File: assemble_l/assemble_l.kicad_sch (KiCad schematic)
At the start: 45 parts, among them J1 Conn_01x02_Pin, SW1 SW_Push, SW10 SW_Push, SW11 SW_Push, SW12 SW_Push, SW13 SW_Push, SW14 SW_Push, SW15 SW_Push, SW16 SW_Push, SW17 SW_Push, SW18 SW_Push, SW19 SW_Push, SW2 SW_Push, SW20 SW_Push, SW21 SW_Push, SW22 SW_Push, SW3 SW_Push, SW4 SW_Push, SW5 SW_Push, SW6 SW_Push, SW7 SW_Push, SW8 SW_Push, SW9 SW_Push, U1 Micon_BLEMicroPro

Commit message: fix: re-change layout
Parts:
- renumbered D9 to D3, D3 to D4, D4 to D5, D5 to D6, D6 to D7, D7 to D8, D8 to D9, SW9 to SW3, SW3 to SW4, SW4 to SW5, SW5 to SW6, SW6 to SW7, SW7 to SW8, SW8 to SW9
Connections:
- net Col0: now also SW3.1
- net Col2: no longer SW3.1
- net Row2: now also D3.1 (K)
- net Row3: no longer D3.1 (K)
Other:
- moved on the sheet: D3, SW3
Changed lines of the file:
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@@
 	)
 	(junction
+		(at 60.96 137.16)
+		(diameter 0)
+		(color 0 0 0 0)
+	)
+	(junction
 		(at 21.59 33.02)
 		(diameter 0)
@@
 	)
 	(junction
-		(at 99.06 158.75)
-		(diameter 0)
-		(color 0 0 0 0)
-	)
-	(junction
 		(at 137.16 158.75)
 		(diameter 0)
@@
 	)
 	(junction
-		(at 88.9 129.54)
+		(at 50.8 113.03)
 		(diameter 0)
 		(color 0 0 0 0)
@@
 	(wire
 		(pts
-			(xy 34.29 137.16) (xy 80.01 137.16)
+			(xy 34.29 137.16) (xy 60.96 137.16)
 		)
 		(stroke
@@
 	(wire
 		(pts
-			(xy 34.29 158.75) (xy 99.06 158.75)
+			(xy 50.8 113.03) (xy 50.8 129.54)
 		)
 		(stroke
@@
 	(wire
 		(pts
-			(xy 121.92 120.65) (xy 137.16 120.65)
+			(xy 34.29 158.75) (xy 121.92 158.75)
 		)
 		(stroke
@@
 	(wire
 		(pts
-			(xy 88.9 129.54) (xy 88.9 147.32)
+			(xy 121.92 120.65) (xy 137.16 120.65)
 		)
 		(stroke
@@
 	(wire
 		(pts
-			(xy 99.06 158.75) (xy 121.92 158.75)
-		)
-		(stroke
-			(width 0)
-			(type default)
-		)
-	)
-	(wire
-		(pts
 			(xy 50.8 93.98) (xy 50.8 113.03)
 		)
@@
 	(wire
 		(pts
-			(xy 99.06 154.94) (xy 99.06 158.75)
+			(xy 60.96 101.6) (xy 80.01 101.6)
 		)
 		(stroke
@@
 	(wire
 		(pts
-			(xy 60.96 101.6) (xy 80.01 101.6)
+			(xy 99.06 137.16) (xy 121.92 137.16)
 		)
 		(stroke
@@
 	(wire
 		(pts
-			(xy 99.06 137.16) (xy 121.92 137.16)
+			(xy 21.59 22.86) (xy 21.59 30.48)
 		)
 		(stroke
@@
 	(wire
 		(pts
-			(xy 21.59 22.86) (xy 21.59 30.48)
+			(xy 137.16 158.75) (xy 153.67 158.75)
 		)
 		(stroke
@@
 	(wire
 		(pts
-			(xy 137.16 158.75) (xy 153.67 158.75)
+			(xy 69.85 93.98) (xy 69.85 113.03)
 		)
 		(stroke
@@
 	(wire
 		(pts
-			(xy 69.85 93.98) (xy 69.85 113.03)
+			(xy 60.96 137.16) (xy 80.01 137.16)
 		)
 		(stroke
@@
 		(dnp no)
 		(fields_autoplaced yes)
-		(property "Reference" "SW8"
+		(property "Reference" "SW9"
 			(at 93.98 121.92 0)
 			(effects
@@
 			(project "wikbd_assemble_l"
 				(path "/d117cd26-8e7e-4c35-b450-26176f9e2abc"
-					(reference "SW8")
+					(reference "SW9")
 					(unit 1)
 				)
@@
 	(symbol
 		(lib_id "Switch:SW_Push")
-		(at 93.98 147.32 0)
+		(at 55.88 129.54 0)
 		(unit 1)
 		(exclude_from_sim no)
@@
 		(dnp no)
 		(fields_autoplaced yes)
-		(property "Reference" "SW9"
-			(at 93.98 139.7 0)
+		(property "Reference" "SW3"
+			(at 55.88 121.92 0)
 			(effects
 				(font
@@
 		)
 		(property "Value" "SW_Push"
-			(at 93.98 142.24 0)
+			(at 55.88 124.46 0)
 			(effects
 				(font
@@
 		)
 		(property "Footprint" "kbd_SW:Choc_v2_Hotswap_1u_16.5"
-			(at 93.98 142.24 0)
+			(at 55.88 124.46 0)
 			(effects
 				(font
@@
 		)
 		(property "Datasheet" "~"
-			(at 93.98 142.24 0)
+			(at 55.88 124.46 0)
 			(effects
 				(font
@@
 		)
 		(property "Description" "Push button switch, generic, two pins"
-			(at 93.98 147.32 0)
+			(at 55.88 129.54 0)
 			(effects
 				(font
@@
 			(project "wikbd_assemble_l"
 				(path "/d117cd26-8e7e-4c35-b450-26176f9e2abc"
-					(reference "SW9")
+					(reference "SW3")
 					(unit 1)
 				)
@@
 		(dnp no)
 		(fields_autoplaced yes)
-		(property "Reference" "D8"
+		(property "Reference" "D9"
 			(at 101.6 132.0799 90)
 			(effects
@@
 			(project "wikbd_assemble_l"
 				(path "/d117cd26-8e7e-4c35-b450-26176f9e2abc"
-					(reference "D8")
+					(reference "D9")
 					(unit 1)
 				)
@@
 		(dnp no)
 		(fields_autoplaced yes)
-		(property "Reference" "D6"
+		(property "Reference" "D7"
 			(at 101.6 96.5199 90)
 			(effects
@@
 			(project "wikbd_assemble_l"
 				(path "/d117cd26-8e7e-4c35-b450-26176f9e2abc"
-					(reference "D6")
+					(reference "D7")
 					(unit 1)
 				)
@@
 		(dnp no)
 		(fields_autoplaced yes)
-		(property "Reference" "D5"
+		(property "Reference" "D6"
 			(at 82.55 132.0799 90)
 			(effects
@@
 			(project "wikbd_assemble_l"
 				(path "/d117cd26-8e7e-4c35-b450-26176f9e2abc"
-					(reference "D5")
+					(reference "D6")
 					(unit 1)
 				)
@@
 		(dnp no)
 		(fields_autoplaced yes)
-		(property "Reference" "SW3"
+		(property "Reference" "SW4"
 			(at 74.93 86.36 0)
 			(effects
@@
 			(project "wikbd_assemble_l"
 				(path "/d117cd26-8e7e-4c35-b450-26176f9e2abc"
-					(reference "SW3")
+					(reference "SW4")
 					(unit 1)
 				)
@@
 		(dnp no)
 		(fields_autoplaced yes)
-		(property "Reference" "SW6"
+		(property "Reference" "SW7"
 			(at 93.98 86.36 0)
 			(effects
@@
 			(project "wikbd_assemble_l"
 				(path "/d117cd26-8e7e-4c35-b450-26176f9e2abc"
-					(reference "SW6")
+					(reference "SW7")
 					(unit 1)
 				)
@@
 	(symbol
 		(lib_id "Device:D")
-		(at 99.06 151.13 90)
+		(at 60.96 133.35 90)
 		(unit 1)
 		(exclude_from_sim no)
@@
 		(dnp no)
 		(fields_autoplaced yes)
-		(property "Reference" "D9"
-			(at 101.6 149.8599 90)
+		(property "Reference" "D3"
+			(at 63.5 132.0799 90)
 			(effects
 				(font
@@
 		)
 		(property "Value" "D"
-			(at 101.6 152.3999 90)
+			(at 63.5 134.6199 90)
 			(effects
 				(font
@@
 		)
 		(property "Footprint" "kbd_Parts:Diode_TH_SMD"
-			(at 99.06 151.13 0)
+			(at 60.96 133.35 0)
 			(effects
 				(font
@@
 		)
 		(property "Datasheet" "~"
-			(at 99.06 151.13 0)
+			(at 60.96 133.35 0)
 			(effects
 				(font
@@
 		)
 		(property "Description" "Diode"
-			(at 99.06 151.13 0)
+			(at 60.96 133.35 0)
 			(effects
 				(font
@@
 		)
 		(property "Sim.Device" "D"
-			(at 99.06 151.13 0)
+			(at 60.96 133.35 0)
 			(effects
 				(font
@@
 		)
 		(property "Sim.Pins" "1=K 2=A"
-			(at 99.06 151.13 0)
+			(at 60.96 133.35 0)
 			(effects
 				(font
@@
 			(project "wikbd_assemble_l"
 				(path "/d117cd26-8e7e-4c35-b450-26176f9e2abc"
-					(reference "D9")
+					(reference "D3")
 					(unit 1)
 				)
@@
 		(dnp no)
 		(fields_autoplaced yes)
-		(property "Reference" "SW5"
+		(property "Reference" "SW6"
 			(at 74.93 121.92 0)
 			(effects
@@
 			(project "wikbd_assemble_l"
 				(path "/d117cd26-8e7e-4c35-b450-26176f9e2abc"
-					(reference "SW5")
+					(reference "SW6")
 					(unit 1)
 				)
@@
 		(dnp no)
 		(fields_autoplaced yes)
-		(property "Reference" "SW4"
+		(property "Reference" "SW5"
 			(at 74.93 105.41 0)
 			(effects
@@
 			(project "wikbd_assemble_l"
 				(path "/d117cd26-8e7e-4c35-b450-26176f9e2abc"
-					(reference "SW4")
+					(reference "SW5")
 					(unit 1)
 				)
@@
 		(dnp no)
 		(fields_autoplaced yes)
-		(property "Reference" "SW7"
+		(property "Reference" "SW8"
 			(at 93.98 105.41 0)
 			(effects
@@
 			(project "wikbd_assemble_l"
 				(path "/d117cd26-8e7e-4c35-b450-26176f9e2abc"
-					(reference "SW7")
+					(reference "SW8")
 					(unit 1)
 				)
@@
 		(dnp no)
 		(fields_autoplaced yes)
-		(property "Reference" "D3"
+		(property "Reference" "D4"
 			(at 82.55 96.5199 90)
 			(effects
@@
 			(project "wikbd_assemble_l"
 				(path "/d117cd26-8e7e-4c35-b450-26176f9e2abc"
-					(reference "D3")
+					(reference "D4")
 					(unit 1)
 				)
@@
 		(dnp no)
 		(fields_autoplaced yes)
-		(property "Reference" "D7"
+		(property "Reference" "D8"
 			(at 101.6 115.5699 90)
 			(effects
@@
 			(project "wikbd_assemble_l"
 				(path "/d117cd26-8e7e-4c35-b450-26176f9e2abc"
-					(reference "D7")
+					(reference "D8")
 					(unit 1)
 				)
@@
 		(dnp no)
 		(fields_autoplaced yes)
-		(property "Reference" "D4"
+		(property "Reference" "D5"
 			(at 82.55 115.5699 90)
 			(effects
@@
 			(project "wikbd_assemble_l"
 				(path "/d117cd26-8e7e-4c35-b450-26176f9e2abc"
-					(reference "D4")
+					(reference "D5")
 					(unit 1)
 				)

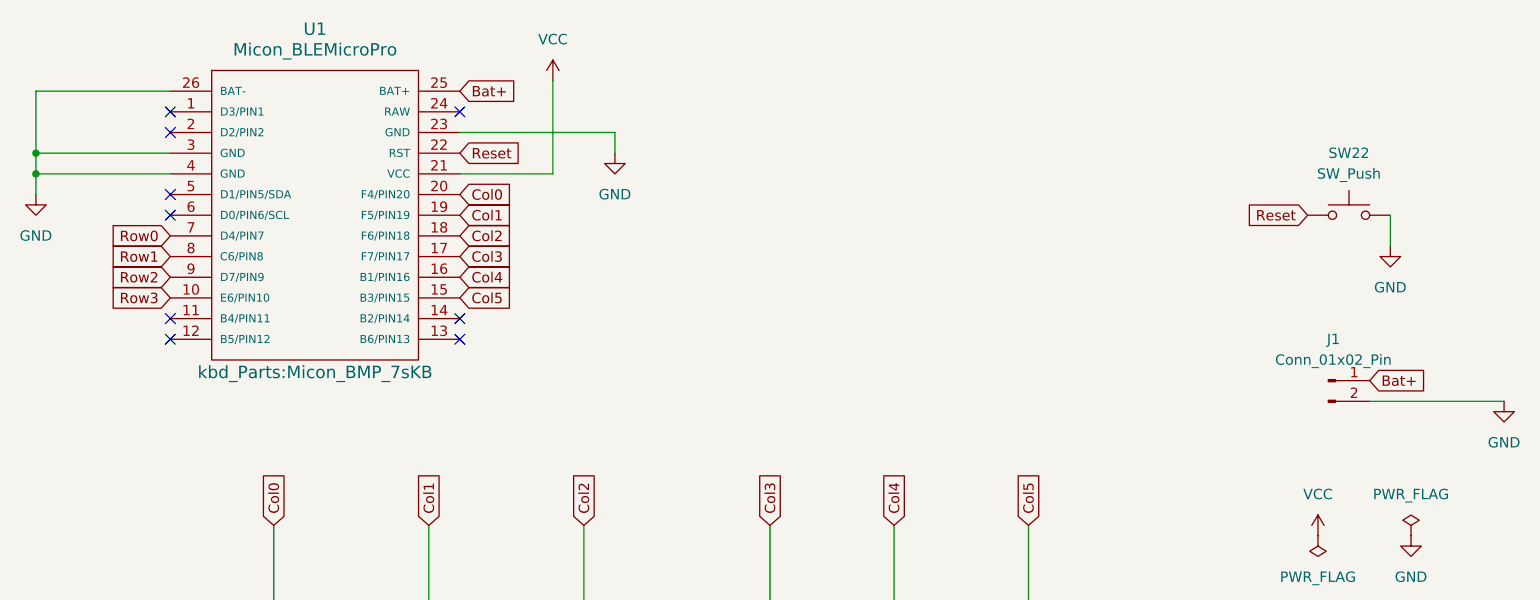
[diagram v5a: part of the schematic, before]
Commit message: feat: add regulation circuit
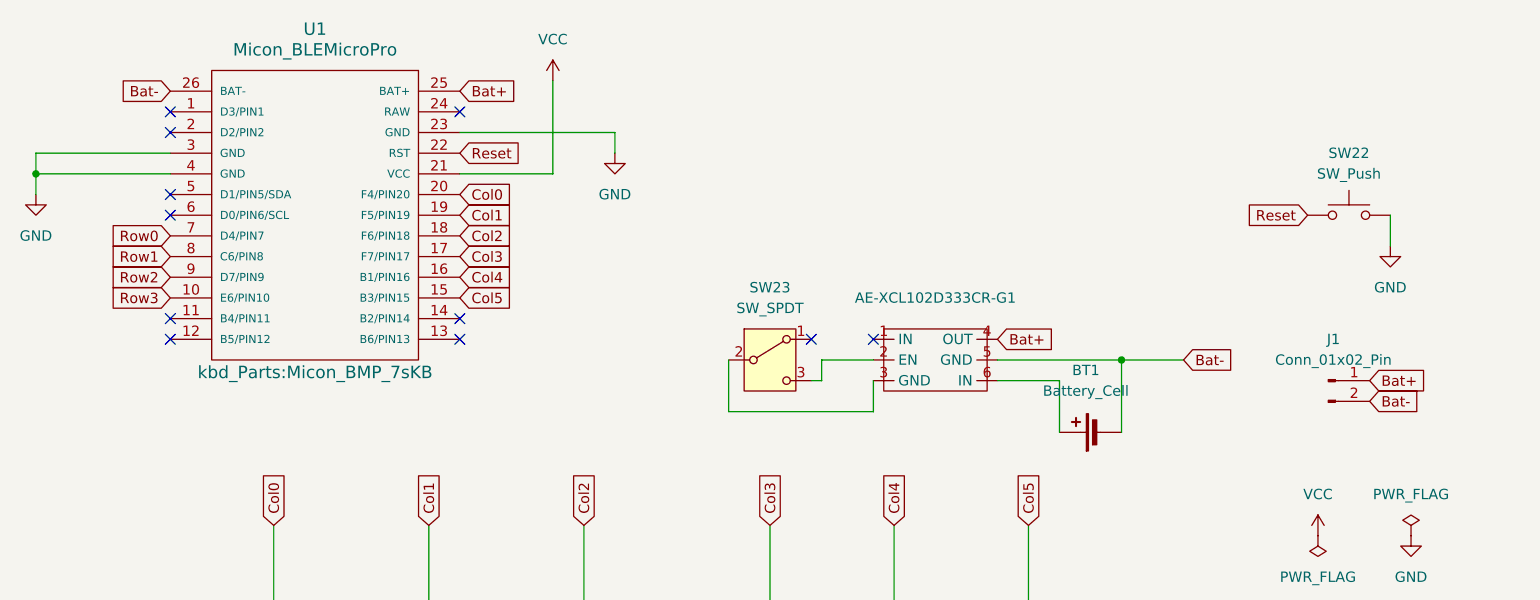
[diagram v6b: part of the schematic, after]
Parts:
- added AE-XCL102D333CR-G1: ~, symbol kicad-lib:AE-XCL102D333CR-G
- added BT1: Battery_Cell, symbol Device:Battery_Cell
- added SW23: SW_SPDT, symbol Switch:SW_SPDT
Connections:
- net Bat+: now also AE-XCL102D333CR-G1.4 (OUT)
- net GND: no longer J1.2 (Pin_2), U1.26 (BAT-)
- new net: AE-XCL102D333CR-G1.2 (EN), SW23.3 (C)
- new net: AE-XCL102D333CR-G1.3 (GND), SW23.2 (B)
- new net: AE-XCL102D333CR-G1.6 (IN), BT1.1 (+)
- new net Bat-: AE-XCL102D333CR-G1.5 (GND), BT1.2 (-), J1.2 (Pin_2), U1.26 (BAT-)
- no-connect marks 9 -> 11

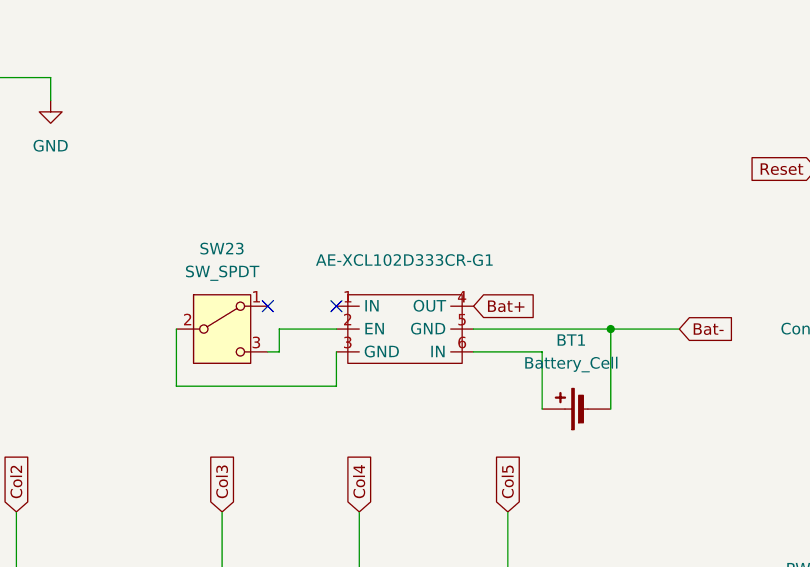
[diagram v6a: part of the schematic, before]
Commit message: feat: update footprint
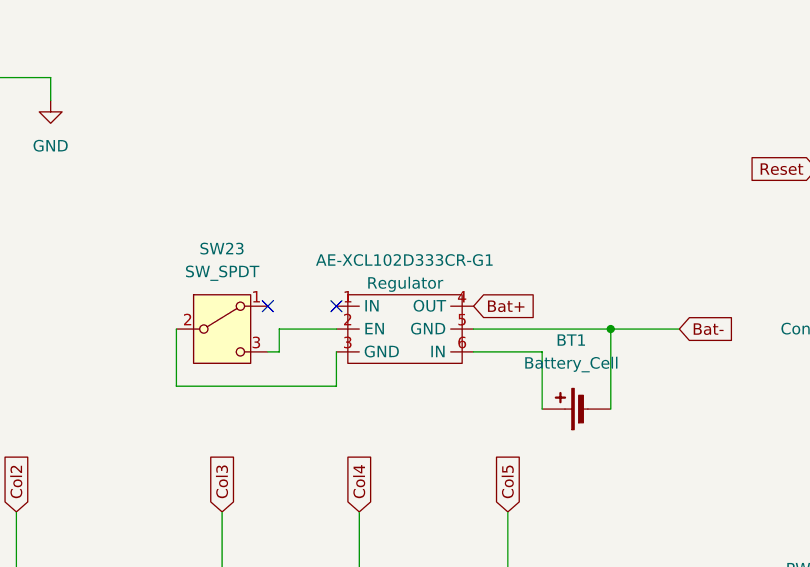
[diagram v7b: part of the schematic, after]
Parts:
- AE-XCL102D333CR-G1: value ~ -> Regulator
- BT1: footprint (none) -> kbd_Parts:Battery_AAA
- SW23: footprint (none) -> kbd_Parts:TGSW_MSK-12D19
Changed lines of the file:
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@@
 			)
 		)
-		(property "Value" "~"
+		(property "Value" "Regulator"
 			(at 132.08 50.8 0)
 			(effects
@@
 			)
 		)
-		(property "Footprint" ""
+		(property "Footprint" "kbd_Parts:TGSW_MSK-12D19"
 			(at 111.76 55.88 0)
 			(effects
@@
 			)
 		)
-		(property "Footprint" ""
+		(property "Footprint" "kbd_Parts:Battery_AAA"
 			(at 150.876 64.77 90)
 			(effects

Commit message: feat: update PCB
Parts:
- removed J1: Conn_01x02_Pin, kbd_Parts:Battery_2pin, symbol Connector:Conn_01x02_Pin
- AE-XCL102D333CR-G1: footprint (none) -> kicad-lib:AE-XCL102D333CR-G
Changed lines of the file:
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@@
 		)
 	)
-	(global_label "Bat-"
+	(global_label "Row2"
 		(shape input)
-		(at 185.42 60.96 0)
+		(at 34.29 137.16 180)
 		(fields_autoplaced yes)
 		(effects
@@
 				(size 1.27 1.27)
 			)
-			(justify left)
+			(justify right)
 		)
 		(property "Intersheetrefs" "${INTERSHEET_REFS}"
-			(at 193.1223 60.96 0)
-			(effects
-				(font
-					(size 1.27 1.27)
-				)
-				(justify left)
-				(hide yes)
-			)
-		)
-	)
-	(global_label "Row2"
+			(at 26.3458 137.16 0)
+			(effects
+				(font
+					(size 1.27 1.27)
+				)
+				(justify right)
+				(hide yes)
+			)
+		)
+	)
+	(global_label "Col5"
 		(shape input)
-		(at 34.29 137.16 180)
+		(at 143.51 76.2 90)
 		(fields_autoplaced yes)
 		(effects
@@
 				(size 1.27 1.27)
 			)
-			(justify right)
+			(justify left)
 		)
 		(property "Intersheetrefs" "${INTERSHEET_REFS}"
-			(at 26.3458 137.16 0)
-			(effects
-				(font
-					(size 1.27 1.27)
-				)
-				(justify right)
+			(at 143.51 68.9211 90)
+			(effects
+				(font
+					(size 1.27 1.27)
+				)
+				(justify left)
 				(hide yes)
 			)
@@
 	(global_label "Col5"
 		(shape input)
-		(at 143.51 76.2 90)
+		(at 73.66 48.26 0)
 		(fields_autoplaced yes)
 		(effects
@@
 		)
 		(property "Intersheetrefs" "${INTERSHEET_REFS}"
-			(at 143.51 68.9211 90)
+			(at 80.9389 48.26 0)
 			(effects
 				(font
@@
 		)
 	)
-	(global_label "Col5"
+	(global_label "Bat-"
 		(shape input)
-		(at 73.66 48.26 0)
+		(at 162.56 55.88 0)
 		(fields_autoplaced yes)
 		(effects
@@
 		)
 		(property "Intersheetrefs" "${INTERSHEET_REFS}"
-			(at 80.9389 48.26 0)
+			(at 170.2623 55.88 0)
 			(effects
 				(font
@@
 		)
 	)
-	(global_label "Bat-"
+	(global_label "Row0"
 		(shape input)
-		(at 162.56 55.88 0)
+		(at 34.29 101.6 180)
 		(fields_autoplaced yes)
 		(effects
@@
 				(size 1.27 1.27)
 			)
-			(justify left)
+			(justify right)
 		)
 		(property "Intersheetrefs" "${INTERSHEET_REFS}"
-			(at 170.2623 55.88 0)
-			(effects
-				(font
-					(size 1.27 1.27)
-				)
-				(justify left)
-				(hide yes)
-			)
-		)
-	)
-	(global_label "Row0"
+			(at 26.3458 101.6 0)
+			(effects
+				(font
+					(size 1.27 1.27)
+				)
+				(justify right)
+				(hide yes)
+			)
+		)
+	)
+	(global_label "Col4"
 		(shape input)
-		(at 34.29 101.6 180)
+		(at 73.66 45.72 0)
 		(fields_autoplaced yes)
 		(effects
@@
 				(size 1.27 1.27)
 			)
-			(justify right)
+			(justify left)
 		)
 		(property "Intersheetrefs" "${INTERSHEET_REFS}"
-			(at 26.3458 101.6 0)
-			(effects
-				(font
-					(size 1.27 1.27)
-				)
-				(justify right)
-				(hide yes)
-			)
-		)
-	)
-	(global_label "Col4"
+			(at 80.9389 45.72 0)
+			(effects
+				(font
+					(size 1.27 1.27)
+				)
+				(justify left)
+				(hide yes)
+			)
+		)
+	)
+	(global_label "Row3"
 		(shape input)
-		(at 73.66 45.72 0)
+		(at 34.29 158.75 180)
 		(fields_autoplaced yes)
 		(effects
@@
 				(size 1.27 1.27)
 			)
-			(justify left)
+			(justify right)
 		)
 		(property "Intersheetrefs" "${INTERSHEET_REFS}"
-			(at 80.9389 45.72 0)
-			(effects
-				(font
-					(size 1.27 1.27)
-				)
-				(justify left)
-				(hide yes)
-			)
-		)
-	)
-	(global_label "Row3"
+			(at 26.3458 158.75 0)
+			(effects
+				(font
+					(size 1.27 1.27)
+				)
+				(justify right)
+				(hide yes)
+			)
+		)
+	)
+	(global_label "Row0"
 		(shape input)
-		(at 34.29 158.75 180)
+		(at 38.1 40.64 180)
 		(fields_autoplaced yes)
 		(effects
@@
 		)
 		(property "Intersheetrefs" "${INTERSHEET_REFS}"
-			(at 26.3458 158.75 0)
-			(effects
-				(font
-					(size 1.27 1.27)
-				)
-				(justify right)
-				(hide yes)
-			)
-		)
-	)
-	(global_label "Row0"
+			(at 30.1558 40.64 0)
+			(effects
+				(font
+					(size 1.27 1.27)
+				)
+				(justify right)
+				(hide yes)
+			)
+		)
+	)
+	(global_label "Col1"
 		(shape input)
-		(at 38.1 40.64 180)
+		(at 73.66 38.1 0)
 		(fields_autoplaced yes)
 		(effects
@@
 				(size 1.27 1.27)
 			)
-			(justify right)
+			(justify left)
 		)
 		(property "Intersheetrefs" "${INTERSHEET_REFS}"
-			(at 30.1558 40.64 0)
-			(effects
-				(font
-					(size 1.27 1.27)
-				)
-				(justify right)
-				(hide yes)
-			)
-		)
-	)
-	(global_label "Bat+"
+			(at 80.9389 38.1 0)
+			(effects
+				(font
+					(size 1.27 1.27)
+				)
+				(justify left)
+				(hide yes)
+			)
+		)
+	)
+	(global_label "Col3"
 		(shape input)
-		(at 185.42 58.42 0)
+		(at 73.66 43.18 0)
 		(fields_autoplaced yes)
 		(effects
@@
 		)
 		(property "Intersheetrefs" "${INTERSHEET_REFS}"
-			(at 193.1223 58.42 0)
+			(at 80.9389 43.18 0)
 			(effects
 				(font
@@
 		)
 	)
-	(global_label "Col1"
+	(global_label "Bat+"
 		(shape input)
-		(at 73.66 38.1 0)
+		(at 139.7 53.34 0)
 		(fields_autoplaced yes)
 		(effects
@@
 		)
 		(property "Intersheetrefs" "${INTERSHEET_REFS}"
-			(at 80.9389 38.1 0)
-			(effects
-				(font
-					(size 1.27 1.27)
-				)
-				(justify left)
-				(hide yes)
-			)
-		)
-	)
-	(global_label "Col3"
-		(shape input)
-		(at 73.66 43.18 0)
-		(fields_autoplaced yes)
-		(effects
-			(font
-				(size 1.27 1.27)
-			)
-			(justify left)
-		)
-		(property "Intersheetrefs" "${INTERSHEET_REFS}"
-			(at 80.9389 43.18 0)
-			(effects
-				(font
-					(size 1.27 1.27)
-				)
-				(justify left)
-				(hide yes)
-			)
-		)
-	)
-	(global_label "Bat+"
-		(shape input)
-		(at 139.7 53.34 0)
-		(fields_autoplaced yes)
-		(effects
-			(font
-				(size 1.27 1.27)
-			)
-			(justify left)
-		)
-		(property "Intersheetrefs" "${INTERSHEET_REFS}"
 			(at 147.4023 53.34 0)
 			(effects
@@
 			)
 		)
-		(property "Footprint" ""
+		(property "Footprint" "kicad-lib:AE-XCL102D333CR-G"
 			(at 132.08 54.61 0)
 			(effects
@@
 					(unit 1)
 				)
-			)
-		)
-	)
-	(symbol
-		(lib_id "Connector:Conn_01x02_Pin")
-		(at 180.34 58.42 0)
-		(unit 1)
-		(exclude_from_sim no)
-		(in_bom yes)
-		(on_board yes)
-		(dnp no)
-		(fields_autoplaced yes)
-		(property "Reference" "J1"
-			(at 180.975 53.34 0)
-			(effects
-				(font
-					(size 1.27 1.27)
-				)
-			)
-		)
-		(property "Value" "Conn_01x02_Pin"
-			(at 180.975 55.88 0)
-			(effects
-				(font
-					(size 1.27 1.27)
-				)
-			)
-		)
-		(property "Footprint" "kbd_Parts:Battery_2pin"
-			(at 180.34 58.42 0)
-			(effects
-				(font
-					(size 1.27 1.27)
-				)
-				(hide yes)
-			)
-		)
-		(property "Datasheet" "~"
-			(at 180.34 58.42 0)
-			(effects
-				(font
-					(size 1.27 1.27)
-				)
-				(hide yes)
-			)
-		)
-		(property "Description" "Generic connector, single row, 01x02, script generated"
-			(at 180.34 58.42 0)
-			(effects
-				(font
-					(size 1.27 1.27)
-				)
-				(hide yes)
-			)
-		)
-		(pin "1"
-		)
-		(pin "2"
-		)
-		(instances
-			(project ""
-				(path "/d117cd26-8e7e-4c35-b450-26176f9e2abc"
-					(reference "J1")
-					(unit 1)
-				)
